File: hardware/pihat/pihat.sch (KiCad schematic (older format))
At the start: 47 parts, among them P1 CONN_13X2

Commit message: More updates, improvements, pihat.
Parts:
- removed SW?: ROTARY_ENCODER_SWITCH, symbol ROTARY_ENCODER_SWITCH
- added RV1: POT, Potentiometers:Potentiometer_Bourns_3296W_3-8Zoll_Inline_ScrewUp, symbol POT
- C1, C11, C2, C3, C4, C5, C6, C7, C8, C9: renamed from C?; footprint (none) -> Capacitors_SMD:C_0805
- C10, C13, C14, C15: renamed from C?; value C -> 10uF; footprint (none) -> Capacitors_SMD:C_0805
- C12: renamed from C?; footprint (none) -> Capacitors_SMD:c_elec_5x5.3
- D1, D2, D3: renamed from D?; footprint (none) -> LEDs:LED_0805
- L1, L2, L3, L4: renamed from L?; footprint (none) -> Resistors_SMD:R_0805
- L5, L6: renamed from L?; footprint (none) -> Choke_Axial_ThroughHole:Choke_Horizontal_RM10mm
- P1: footprint (none) -> Pin_Headers:Pin_Header_Angled_2x13
- P2: renamed from P?; footprint (none) -> Connect:USB_Micro-B
- P3: renamed from P?; footprint (none) -> Pin_Headers:Pin_Header_Straight_1x02
- R1, R2, R3, R4, R5: renamed from R?; footprint (none) -> Resistors_SMD:R_0805
- R10, R11, R6, R7, R8, R9: renamed from R?; footprint (none) -> Resistors_SMD:R_0603
- TH1: renamed from TH?; footprint (none) -> Resistors_SMD:R_0805
- U1: renamed from U?; footprint (none) -> Housings_DFN_QFN:DFN-8-1EP_3x3mm_Pitch0.5mm
- U2: renamed from U?; footprint (none) -> Housings_DFN_QFN:DFN-10-1EP_3x3mm_Pitch0.5mm
- U3: renamed from U?; footprint (none) -> Housings_DFN_QFN:DFN-6-1EP_2x2mm_Pitch0.5mm
- U4: renamed from U?; footprint (none) -> Housings_DFN_QFN:QFN-20-1EP_4x4mm_Pitch0.5mm
- X1: renamed from X?; footprint (none) -> Crystals:Crystal_SMD_5032_4Pads
- gave numbers to parts that had none: 2
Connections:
- net GPIO22 is gone; now on net VOL: P1.15 (P15)
- net +5V: now also RV1.3
- net GND: now also RV1.2
- net VOL: now also RV1.1

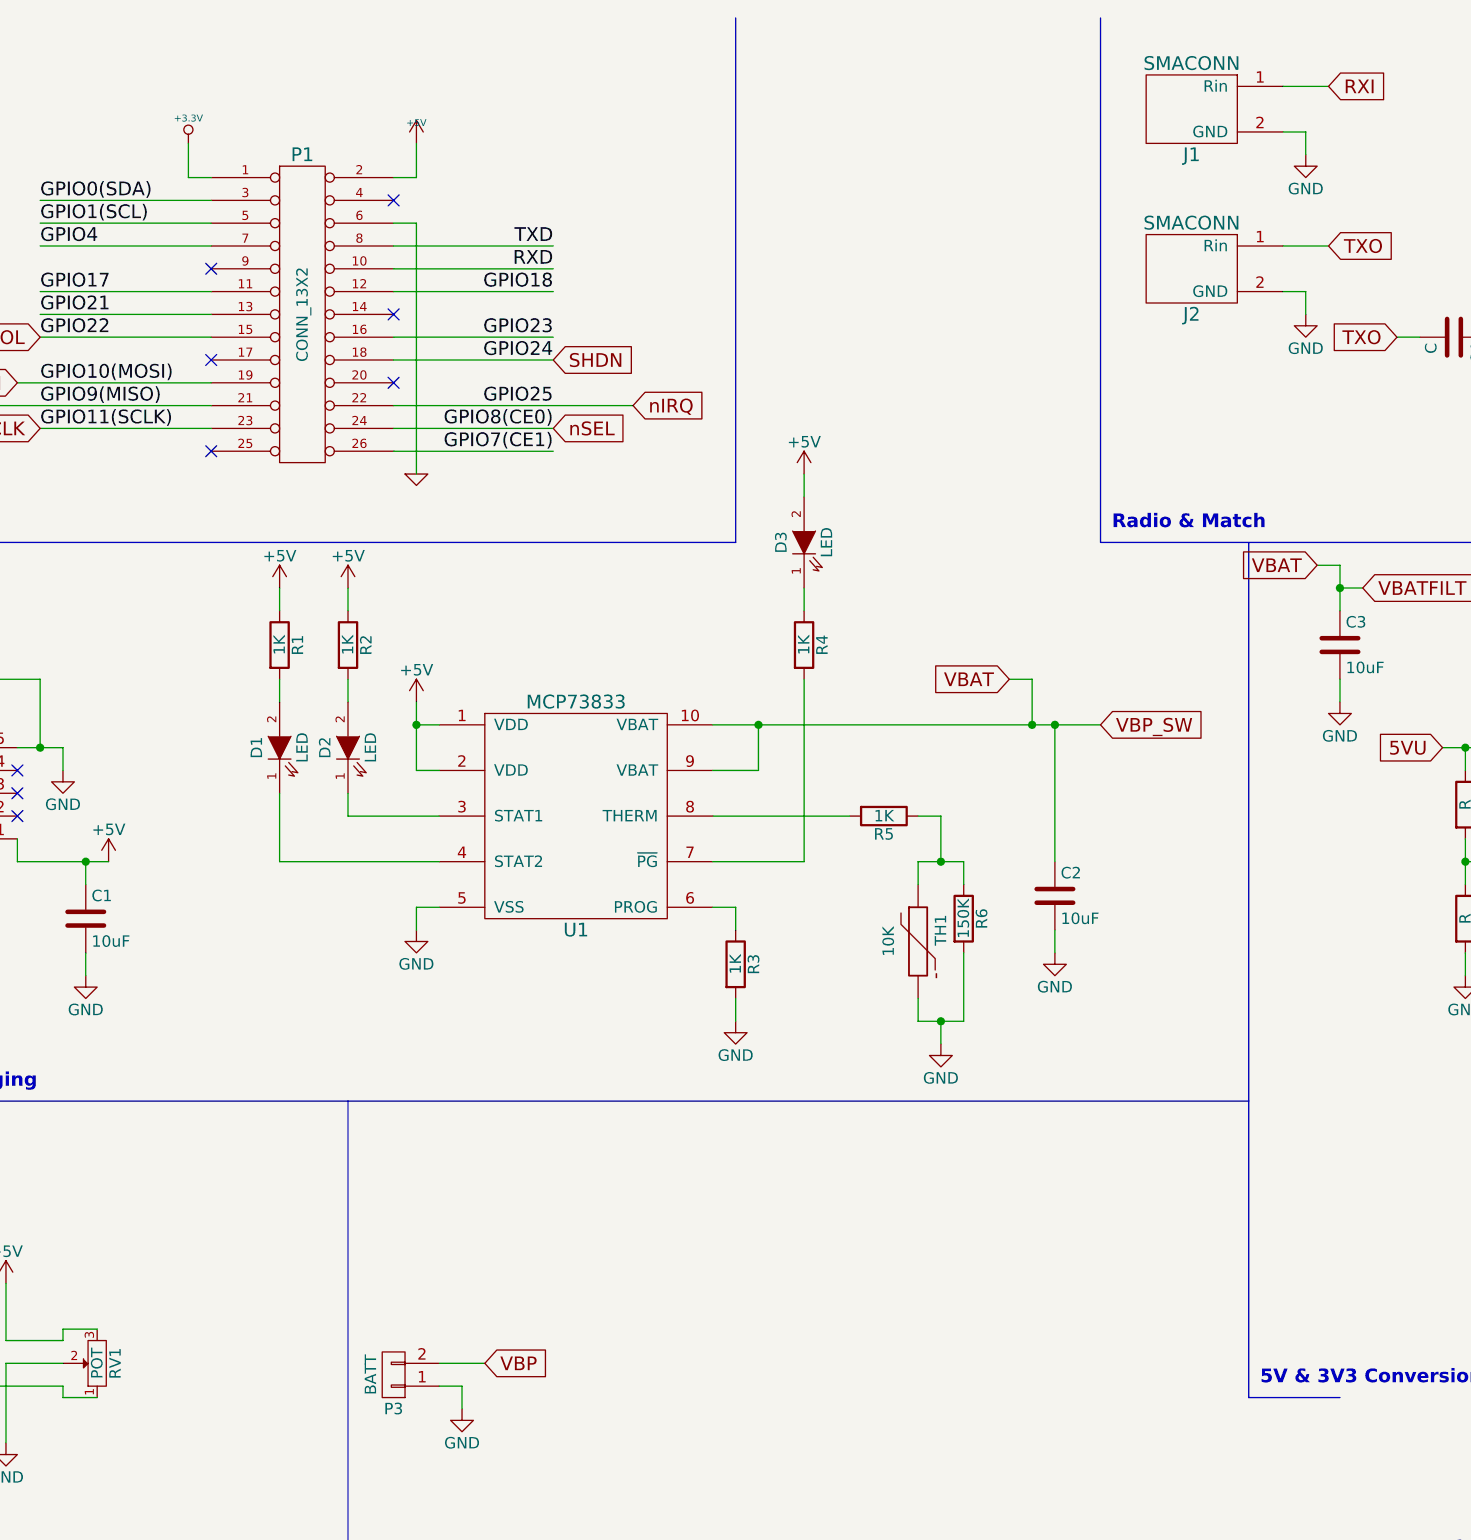
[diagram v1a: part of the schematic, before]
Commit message: Added a bit more to the routing.
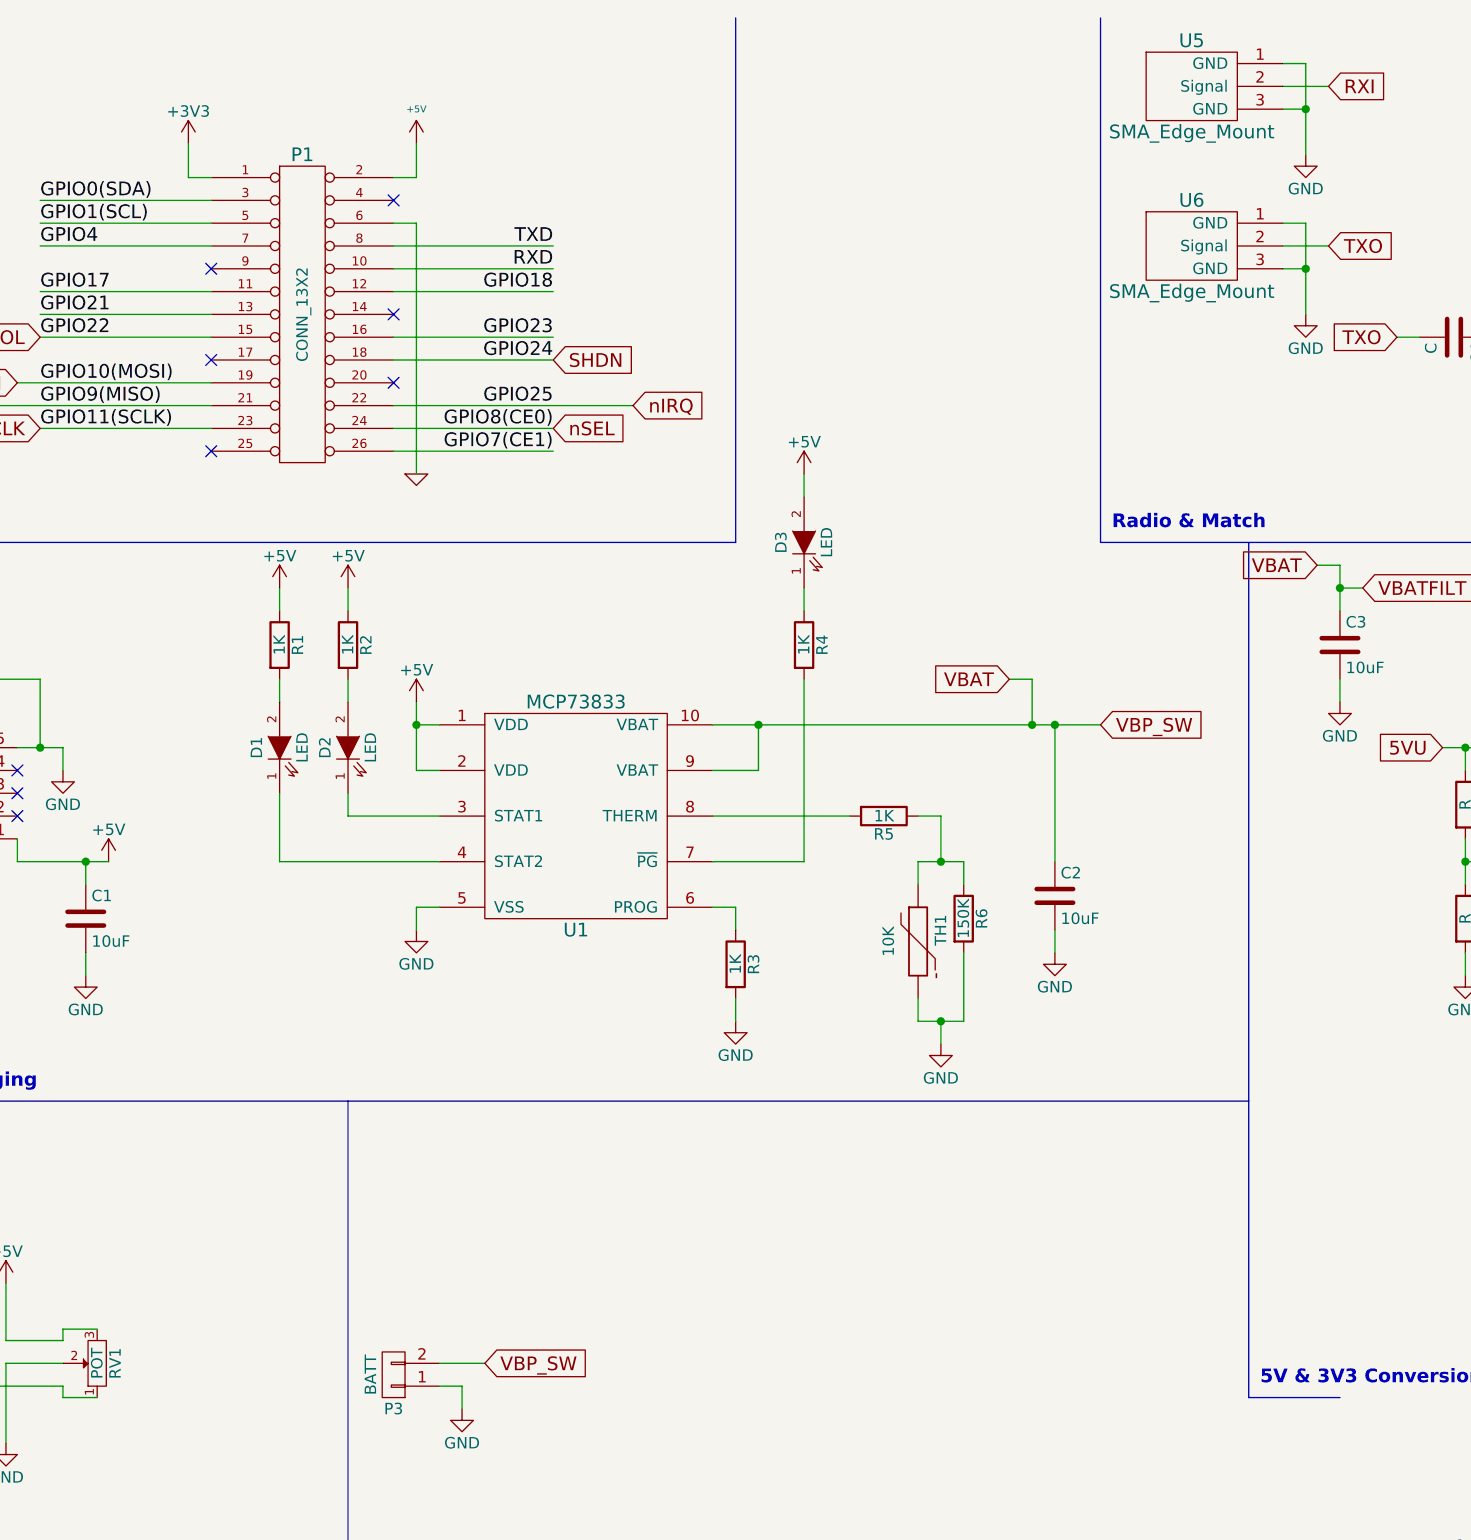
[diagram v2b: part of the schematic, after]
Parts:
- removed J1, J2: SMACONN, symbol SMACONN
- added U5, U6: SMA_Edge_Mount, RF BW Filter:SMA_Edge_Mount, symbol SMA_Edge_Mount
- P1: footprint Pin_Headers:Pin_Header_Angled_2x13 -> Pin_Headers:Pin_Header_Straight_2x13
- U1: footprint Housings_DFN_QFN:DFN-8-1EP_3x3mm_Pitch0.5mm -> Housings_DFN_QFN:DFN-10-1EP_3x3mm_Pitch0.5mm
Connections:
- net +3.3V is gone; now on net +3V3: P1.1 (P1)
- net VBP is gone; now on net VBAT: P3.2 (P2)
- net GND: now also U5.1 (GND), U5.3 (GND), U6.1 (GND), U6.3 (GND)
- net RXI: now also U5.2 (Signal)
- net TXO: now also U6.2 (Signal)
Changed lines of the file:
@@
 LIBS:RFT
 LIBS:PWR
+LIBS:RF BW Filter Library
 LIBS:pihat-cache
 EELAYER 25 0
@@
 F 0 "P1" H 2400 2500 60  0000 C CNN
 F 1 "CONN_13X2" V 2400 1800 50  0000 C CNN
-F 2 "Pin_Headers:Pin_Header_Angled_2x13" H 2400 1800 60  0001 C CNN
+F 2 "Pin_Headers:Pin_Header_Straight_2x13" H 2400 1800 60  0001 C CNN
 F 3 "" H 2400 1800 60  0001 C CNN
 	1    2400 1800
-	1    0    0    -1
-$EndComp
-$Comp
-L +3.3V-RESCUE-pihat #PWR01
-U 1 1 50A55B18
-P 1900 1050
-F 0 "#PWR01" H 1900 1010 30  0001 C CNN
-F 1 "+3.3V" H 1900 1160 30  0000 C CNN
-F 2 "" H 1900 1050 60  0001 C CNN
-F 3 "" H 1900 1050 60  0001 C CNN
-	1    1900 1050
 	1    0    0    -1
 $EndComp
@@
 P 2900 1050
 F 0 "#PWR02" H 2900 1140 20  0001 C CNN
-F 1 "+5V" H 2900 1140 30  0000 C CNN
+F 1 "+5V" H 2900 1200 30  0000 C CNN
 F 2 "" H 2900 1050 60  0001 C CNN
 F 3 "" H 2900 1050 60  0001 C CNN
@@
 F 3 "" H 9750 1800 60  0001 C CNN
 	1    9750 1800
-	1    0    0    -1
-$EndComp
-$Comp
-L SMACONN J1
-U 1 1 58D583F0
-P 6300 900
-F 0 "J1" H 6300 700 60  0000 C CNN
-F 1 "SMACONN" H 6300 1100 60  0000 C CNN
-F 2 "" H 6300 900 60  0001 C CNN
-F 3 "" H 6300 900 60  0001 C CNN
-	1    6300 900
-	1    0    0    -1
-$EndComp
-$Comp
-L SMACONN J2
-U 1 1 58D58491
-P 6300 1600
-F 0 "J2" H 6300 1400 60  0000 C CNN
-F 1 "SMACONN" H 6300 1800 60  0000 C CNN
-F 2 "" H 6300 1600 60  0001 C CNN
-F 3 "" H 6300 1600 60  0001 C CNN
-	1    6300 1600
 	1    0    0    -1
 $EndComp
@@
 TXO
 Wire Wire Line
-	6700 1700 6800 1700
-Wire Wire Line
-	6800 1700 6800 1800
+	6800 1400 6800 1800
 $Comp
 L GND #PWR010
@@
 $EndComp
 Wire Wire Line
-	6700 1000 6800 1000
-Wire Wire Line
-	6800 1000 6800 1100
+	6800 700  6800 1100
 $Comp
 L GND #PWR011
@@
 F 0 "U1" H 3600 3500 60  0000 C CNN
 F 1 "MCP73833" H 3600 4500 60  0000 C CNN
-F 2 "Housings_DFN_QFN:DFN-8-1EP_3x3mm_Pitch0.5mm" H 3600 4000 60  0001 C CNN
+F 2 "Housings_DFN_QFN:DFN-10-1EP_3x3mm_Pitch0.5mm" H 3600 4000 60  0001 C CNN
 F 3 "" H 3600 4000 60  0001 C CNN
 	1    3600 4000
@@
 	3000 6400 3200 6400
 Text GLabel 3200 6400 2    60   Input ~ 0
-VBP
+VBP_SW
 Text Notes 7350 7500 0    60   Italic 12
 Pi Hat Schematic
@@
 Text GLabel 1250 1900 0    60   Input ~ 0
 VOL
+$Comp
+L SMA_Edge_Mount U6
+U 1 1 58E16429
+P 6300 1500
+F 0 "U6" H 6300 1700 60  0000 C CNN
+F 1 "SMA_Edge_Mount" H 6300 1300 60  0000 C CNN
+F 2 "RF BW Filter:SMA_Edge_Mount" H 6300 1500 60  0001 C CNN
+F 3 "" H 6300 1500 60  0001 C CNN
+	1    6300 1500
+	1    0    0    -1
+$EndComp
+Wire Wire Line
+	6700 1400 6800 1400
+Wire Wire Line
+	6700 1600 6800 1600
+Connection ~ 6800 1600
+$Comp
+L SMA_Edge_Mount U5
+U 1 1 58E16778
+P 6300 800
+F 0 "U5" H 6300 1000 60  0000 C CNN
+F 1 "SMA_Edge_Mount" H 6300 600 60  0000 C CNN
+F 2 "RF BW Filter:SMA_Edge_Mount" H 6300 800 60  0001 C CNN
+F 3 "" H 6300 800 60  0001 C CNN
+	1    6300 800
+	1    0    0    -1
+$EndComp
+Wire Wire Line
+	6700 700  6800 700
+Wire Wire Line
+	6800 900  6700 900
+Connection ~ 6800 900
+$Comp
+L +3V3 #PWR?
+U 1 1 58E1AE94
+P 1900 1050
+F 0 "#PWR?" H 1900 900 50  0001 C CNN
+F 1 "+3V3" H 1900 1190 50  0000 C CNN
+F 2 "" H 1900 1050 50  0000 C CNN
+F 3 "" H 1900 1050 50  0000 C CNN
+	1    1900 1050
+	1    0    0    -1
+$EndComp
 $EndSCHEMATC

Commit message: Prepared new Board.
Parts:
- added C16, C17: 10nF, Capacitors_SMD:C_0805, symbol C
- added P?: CONN_02X20, symbol CONN_02X20
- L5, L6: footprint Choke_Axial_ThroughHole:Choke_Horizontal_RM10mm -> inductor:BOURNES_SRN4018
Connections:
- net +3V3: now also C16.2, C17.2, P?.1 (P1), P?.17 (P17); no longer P1.1 (P1)
- net +5V: now also C10.1, C13.1, U3.1 (VIN), U3.3 (EN), P?.2 (P2), P?.4 (P4); no longer P1.2 (P2)
- net GND: now also RV1.1, C16.1, C17.1, P?.14 (P14), P?.39 (P39), P?.9 (P9); no longer P1.6 (P6), RV1.2
- net VBAT: no longer C10.1, C13.1, U3.1 (VIN), U3.3 (EN)
- net VOL: now also RV1.2; no longer RV1.1
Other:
- moved on the sheet: P1
